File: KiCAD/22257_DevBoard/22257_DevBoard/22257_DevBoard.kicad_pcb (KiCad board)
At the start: 6 copper layers, 5 parts, among them U3 TPS73633DBV, U4 TPS562202, U5 INA219AxD, U6 INA219AxD, U7 BME680

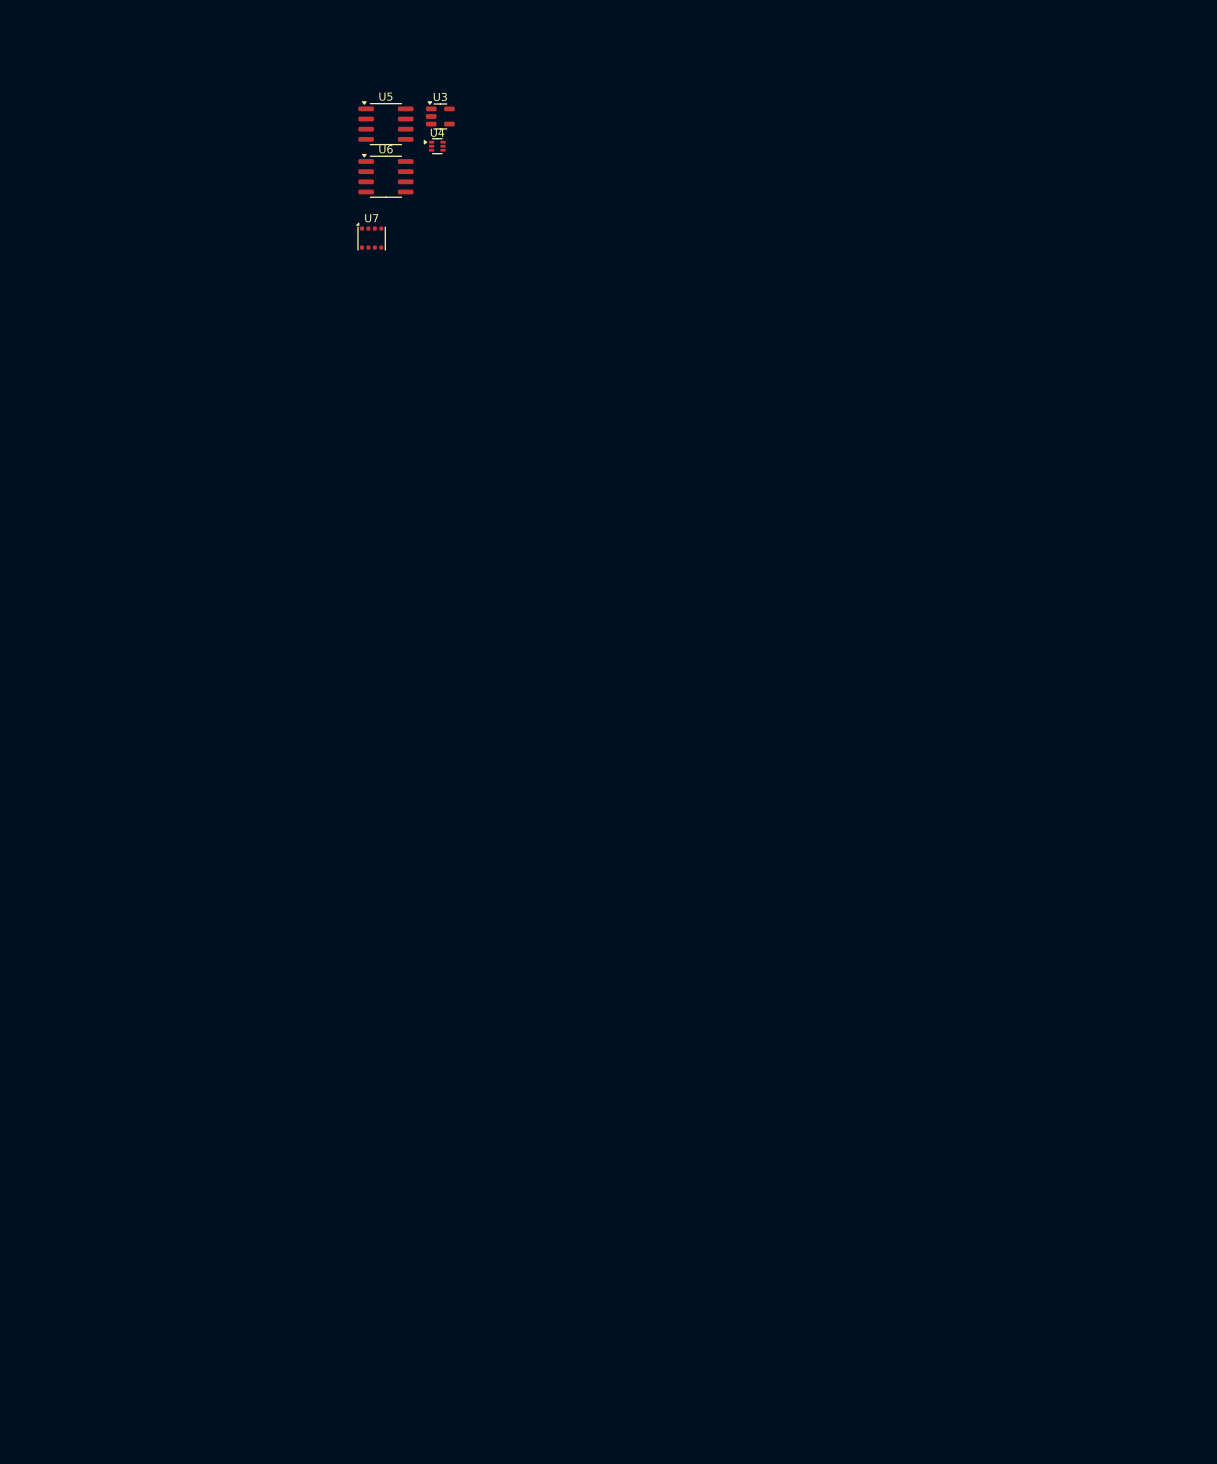
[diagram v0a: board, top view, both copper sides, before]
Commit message: Started layout
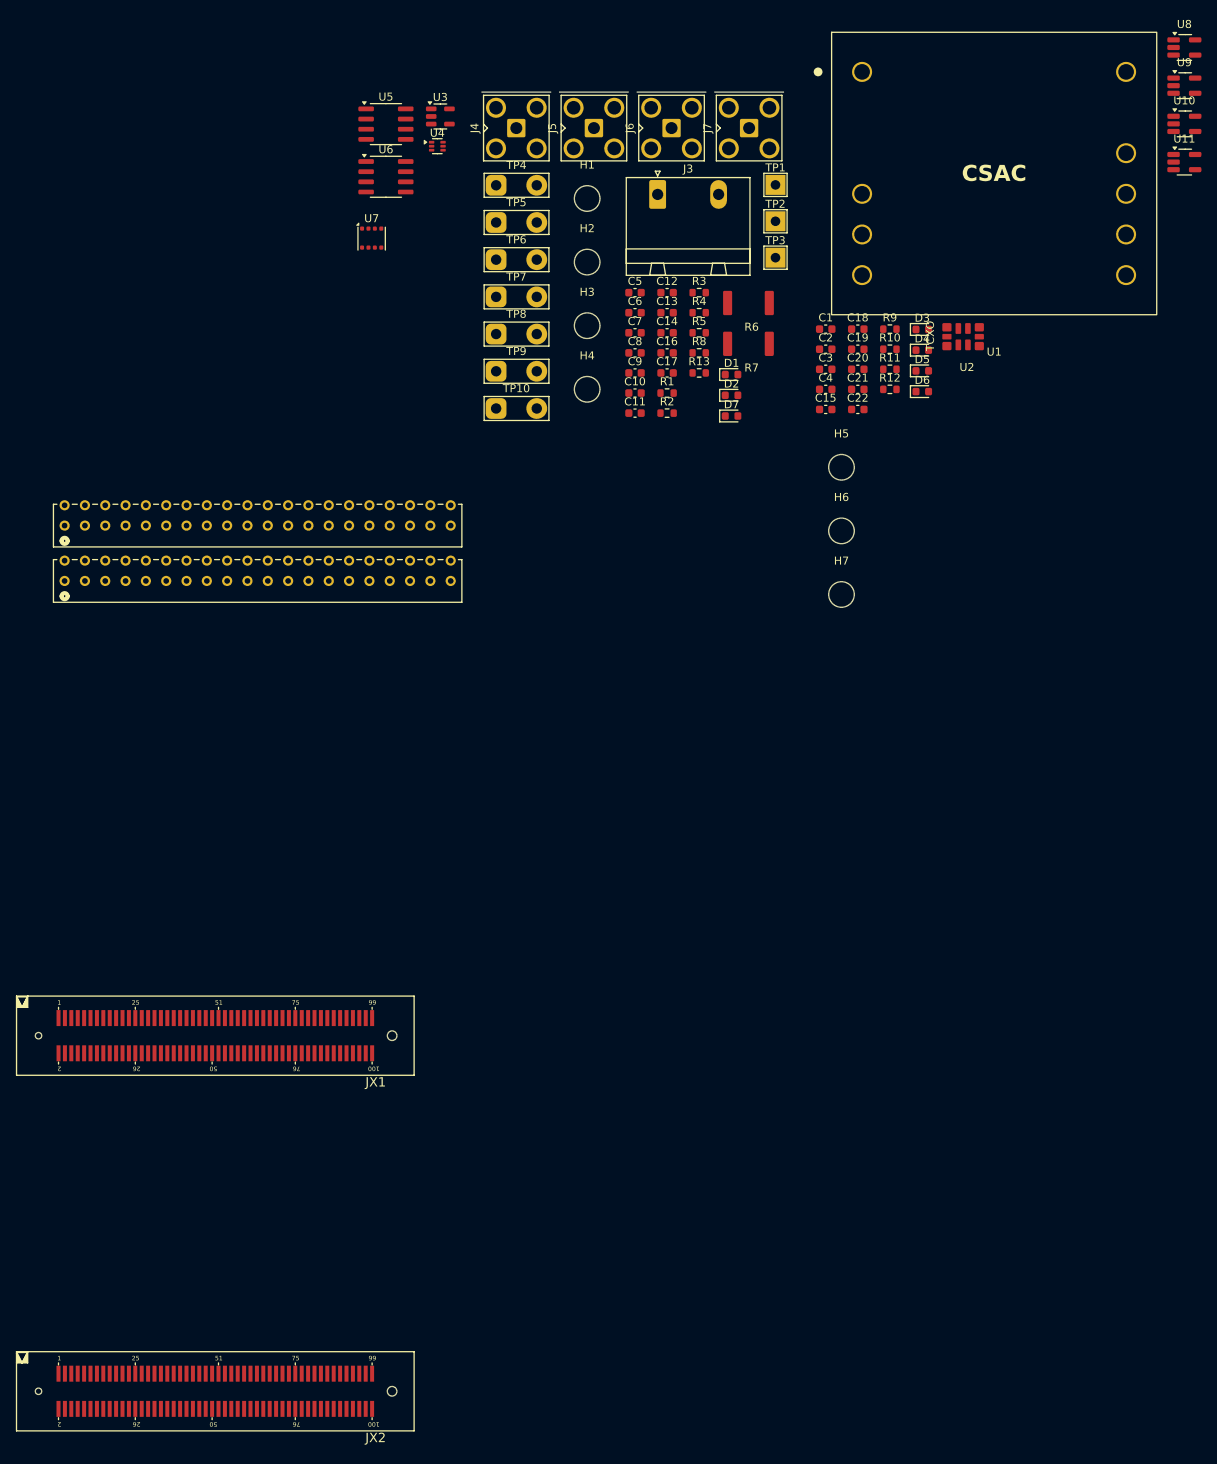
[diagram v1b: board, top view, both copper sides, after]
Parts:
- added C1: 0.01u, Capacitor_SMD:C_0603_1608Metric, F.Cu at (58.7, 28.5)
- added C10: 0.1u, Capacitor_SMD:C_0603_1608Metric, F.Cu at (34.9, 36.5)
- added C11: 22u, Capacitor_SMD:C_0603_1608Metric, F.Cu at (34.9, 39.0)
- added C12: 22u, Capacitor_SMD:C_0603_1608Metric, F.Cu at (38.9, 23.9)
- added C13: 22u, Capacitor_SMD:C_0603_1608Metric, F.Cu at (38.9, 26.4)
- added C14: .1u, Capacitor_SMD:C_0603_1608Metric, F.Cu at (38.9, 28.9)
- added C15: 4.7u, Capacitor_SMD:C_0603_1608Metric, F.Cu at (58.7, 38.5)
- added C16: 0.01u, Capacitor_SMD:C_0603_1608Metric, F.Cu at (38.9, 31.4)
- added C17: 0.01u, Capacitor_SMD:C_0603_1608Metric, F.Cu at (38.9, 34.0)
- added C18: 0.01u, Capacitor_SMD:C_0603_1608Metric, F.Cu at (62.7, 28.5)
- added C19: 0.01u, Capacitor_SMD:C_0603_1608Metric, F.Cu at (62.7, 31.0)
- added C2: 4.7u, Capacitor_SMD:C_0603_1608Metric, F.Cu at (58.7, 31.0)
- added C20: 0.01u, Capacitor_SMD:C_0603_1608Metric, F.Cu at (62.7, 33.5)
- added C21: 0.01u, Capacitor_SMD:C_0603_1608Metric, F.Cu at (62.7, 36.0)
- added C22: 0.01u, Capacitor_SMD:C_0603_1608Metric, F.Cu at (62.7, 38.5)
- added C3: 4.7u, Capacitor_SMD:C_0603_1608Metric, F.Cu at (58.7, 33.5)
- added C4: 0.01u, Capacitor_SMD:C_0603_1608Metric, F.Cu at (58.7, 36.0)
- added C5: 10n, Capacitor_SMD:C_0603_1608Metric, F.Cu at (34.9, 23.9)
- added C6: 10u, Capacitor_SMD:C_0603_1608Metric, F.Cu at (34.9, 26.4)
- added C7: 0.1u, Capacitor_SMD:C_0603_1608Metric, F.Cu at (34.9, 28.9)
- added C8: 10u, Capacitor_SMD:C_0603_1608Metric, F.Cu at (34.9, 31.4)
- added C9: 4.7u, Capacitor_SMD:C_0603_1608Metric, F.Cu at (34.9, 34.0)
- added D1: LED, LED_SMD:LED_0603_1608Metric, F.Cu at (46.9, 34.2)
- added D2: LED, LED_SMD:LED_0603_1608Metric, F.Cu at (46.9, 36.8)
- added D3: LED, LED_SMD:LED_0603_1608Metric, F.Cu at (70.8, 28.5)
- added D4: LED, LED_SMD:LED_0603_1608Metric, F.Cu at (70.8, 31.1)
- added D5: LED, LED_SMD:LED_0603_1608Metric, F.Cu at (70.8, 33.7)
- added D6: LED, LED_SMD:LED_0603_1608Metric, F.Cu at (70.8, 36.3)
- added D7: LED, LED_SMD:LED_0603_1608Metric, F.Cu at (46.9, 39.3)
- added H1: MOUNT-PAD-ROUND5.0, MountingHole:MountingHole_3.2mm_M3, F.Cu at (28.9, 12.2)
- added H2: MOUNT-PAD-ROUND5.0, MountingHole:MountingHole_3.2mm_M3, F.Cu at (28.9, 20.1)
- added H3: MOUNT-PAD-ROUND5.0, MountingHole:MountingHole_3.2mm_M3, F.Cu at (28.9, 28.1)
- added H4: MOUNT-PAD-ROUND5.0, MountingHole:MountingHole_3.2mm_M3, F.Cu at (28.9, 36.0)
- added H5: MOUNT-PAD-ROUND5.0, MountingHole:MountingHole_3.2mm_M3, F.Cu at (60.7, 45.8)
- added H6: MOUNT-PAD-ROUND5.0, MountingHole:MountingHole_3.2mm_M3, F.Cu at (60.7, 53.7)
- added H7: MOUNT-PAD-ROUND5.0, MountingHole:MountingHole_3.2mm_M3, F.Cu at (60.7, 61.6)
- added J1: TD-120-G-AACON40_2X20_TU_HTS_SAI, 22257_DevBoard:CON40_2X20_TU_HTS_SAI, F.Cu at (-12.3, 51.8)
- added J2: TD-120-G-AACON40_2X20_TU_HTS_SAI, 22257_DevBoard:CON40_2X20_TU_HTS_SAI, F.Cu at (-12.3, 58.7)
- added J3: Screw_Terminal_01x02, Connector_Phoenix_GMSTB:PhoenixContact_GMSTBA_2,5_2-G-7,62_1x02_P7.62mm_Horizontal, F.Cu at (37.7, 11.6)
- added J4: Conn_Coaxial, Connector_Coaxial:SMA_Amphenol_901-143_Horizontal, F.Cu at (20.0, 3.35)
- added J5: Conn_Coaxial, Connector_Coaxial:SMA_Amphenol_901-143_Horizontal, F.Cu at (29.7, 3.35)
- added J6: Conn_Coaxial, Connector_Coaxial:SMA_Amphenol_901-143_Horizontal, F.Cu at (39.4, 3.35)
- added J7: Conn_Coaxial, Connector_Coaxial:SMA_Amphenol_901-143_Horizontal, F.Cu at (49.1, 3.35)
- added JX1: 61083-102402LF, 22257_DevBoard:61083-102402LF_1104291, F.Cu at (-39.7, 116.8)
- added JX2: 61083-102402LF, 22257_DevBoard:61083-102402LF_1104291, F.Cu at (-39.7, 161.3)
- added R1: 200k, Resistor_SMD:R_0603_1608Metric, F.Cu at (38.9, 36.5)
- added R10: 1k, Resistor_SMD:R_0603_1608Metric, F.Cu at (66.7, 31.0)
- added R11: 1k, Resistor_SMD:R_0603_1608Metric, F.Cu at (66.7, 33.5)
- added R12: 1k, Resistor_SMD:R_0603_1608Metric, F.Cu at (66.7, 36.0)
- added R13: 1k, Resistor_SMD:R_0603_1608Metric, F.Cu at (42.9, 34.0)
- added R2: 1k, Resistor_SMD:R_0603_1608Metric, F.Cu at (38.9, 39.0)
- added R3: 10k, Resistor_SMD:R_0603_1608Metric, F.Cu at (42.9, 23.9)
- added R4: 52.3k, Resistor_SMD:R_0603_1608Metric, F.Cu at (42.9, 26.4)
- added R5: 10k, Resistor_SMD:R_0603_1608Metric, F.Cu at (42.9, 28.9)
- added R6: R_Shunt_US, 2222_DevBoar_Footprints:BVT-I-R0002-1, F.Cu at (46.4, 25.2)
- added R7: R_Shunt_US, 2222_DevBoar_Footprints:BVT-I-R0002-1, F.Cu at (46.4, 30.3)
- added R8: 1k, Resistor_SMD:R_0603_1608Metric, F.Cu at (42.9, 31.4)
- added R9: 1k, Resistor_SMD:R_0603_1608Metric, F.Cu at (66.7, 28.5)
- added TP1: TestPoint, TestPoint:TestPoint_THTPad_2.5x2.5mm_Drill1.2mm, F.Cu at (52.4, 10.4)
- added TP10: TestPoint_2Pole, TestPoint:TestPoint_2Pads_Pitch5.08mm_Drill1.3mm, F.Cu at (17.5, 38.4)
- added TP2: TestPoint, TestPoint:TestPoint_THTPad_2.5x2.5mm_Drill1.2mm, F.Cu at (52.4, 15.0)
- added TP3: TestPoint, TestPoint:TestPoint_THTPad_2.5x2.5mm_Drill1.2mm, F.Cu at (52.4, 19.6)
- added TP4: TestPoint_2Pole, TestPoint:TestPoint_2Pads_Pitch5.08mm_Drill1.3mm, F.Cu at (17.5, 10.5)
- added TP5: TestPoint_2Pole, TestPoint:TestPoint_2Pads_Pitch5.08mm_Drill1.3mm, F.Cu at (17.5, 15.2)
- added TP6: TestPoint_2Pole, TestPoint:TestPoint_2Pads_Pitch5.08mm_Drill1.3mm, F.Cu at (17.5, 19.8)
- added TP7: TestPoint_2Pole, TestPoint:TestPoint_2Pads_Pitch5.08mm_Drill1.3mm, F.Cu at (17.5, 24.4)
- added TP8: TestPoint_2Pole, TestPoint:TestPoint_2Pads_Pitch5.08mm_Drill1.3mm, F.Cu at (17.5, 29.1)
- added TP9: TestPoint_2Pole, TestPoint:TestPoint_2Pads_Pitch5.08mm_Drill1.3mm, F.Cu at (17.5, 33.8)
- added U1: ~, 2222_DevBoar_Footprints:SA-45, F.Cu at (63.2, -3.67)
- added U10: 74LVC1G17, Package_TO_SOT_SMD:SOT-23-5_HandSoldering, F.Cu at (103.5, 2.83)
- added U11: 74LVC1G17, Package_TO_SOT_SMD:SOT-23-5_HandSoldering, F.Cu at (103.5, 7.60)
- added U2: ~, 2222_DevBoar_Footprints:SiT5356, F.Cu at (73.8, 28.2)
- added U8: 74LVC1G17, Package_TO_SOT_SMD:SOT-23-5_HandSoldering, F.Cu at (103.5, -6.72)
- added U9: 74LVC1G17, Package_TO_SOT_SMD:SOT-23-5_HandSoldering, F.Cu at (103.5, -1.95)

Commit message: Finished Component Placement and Arrangement.
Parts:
- removed H5, H6, H7: MOUNT-PAD-ROUND5.0, MountingHole:MountingHole_3.2mm_M3
- added H10: MountingHole_Pad, MountingHole:MountingHole_3.2mm_M3_Pad, F.Cu at (12.8, 19.1)
- added H11: MountingHole_Pad, MountingHole:MountingHole_3.2mm_M3_Pad, F.Cu at (12.8, 68.6)
- added H8: MountingHole_Pad, MountingHole:MountingHole_3.2mm_M3_Pad, F.Cu at (106.8, 68.6)
- added H9: MountingHole_Pad, MountingHole:MountingHole_3.2mm_M3_Pad, F.Cu at (106.8, 19.1)
- added L1: 10u, Inductor_SMD:L_Bourns-SRU8043, F.Cu at (149.3, 2.62)
- added L2: 4.7u, Inductor_SMD:L_Bourns-SRU8043, F.Cu at (166.2, 2.79)
- added TP11: TestPoint, TestPoint:TestPoint_THTPad_2.5x2.5mm_Drill1.2mm, F.Cu at (162.8, 33.3)
- added TP12: TestPoint, TestPoint:TestPoint_THTPad_2.5x2.5mm_Drill1.2mm, F.Cu at (97.8, 81.3)
- added TP13: TestPoint, TestPoint:TestPoint_THTPad_2.5x2.5mm_Drill1.2mm, F.Cu at (29.2, 5.54)
- added TP14: TestPoint, TestPoint:TestPoint_THTPad_2.5x2.5mm_Drill1.2mm, F.Cu at (104.3, 1.56)
- added TP15: TestPoint, TestPoint:TestPoint_THTPad_2.5x2.5mm_Drill1.2mm, F.Cu at (155.7, 25.7)
- added TP16: TestPoint, TestPoint:TestPoint_THTPad_2.5x2.5mm_Drill1.2mm, F.Cu at (155.7, 29.7)
- added TP17: TestPoint, TestPoint:TestPoint_THTPad_2.5x2.5mm_Drill1.2mm, F.Cu at (128.5, 22.1)
- added TP18: TestPoint, TestPoint:TestPoint_THTPad_2.5x2.5mm_Drill1.2mm, F.Cu at (128.5, 26.2)
- H1, H2, H3, H4: value MOUNT-PAD-ROUND5.0 -> MountingHole_Pad; footprint MountingHole:MountingHole_3.2mm_M3 -> MountingHole:MountingHole_3.2mm_M3_Pad
- moved J4 183.2 mm to (201.9, 25.4), turned to -90 degrees
- moved TP5 182.8 mm to (193.0, 66.0), turned to -90 degrees
- moved H4 182.2 mm to (203.2, 88.9)
- moved TP4 180.1 mm to (193.0, 50.8), turned to -90 degrees
- moved H3 176.6 mm to (203.2, 0.00)
- moved TP7 176.3 mm to (193.0, 40.6), turned to 90 degrees
- moved J5 176.2 mm to (201.9, 40.6), turned to -90 degrees
- moved TP6 175.6 mm to (193.0, 25.4), turned to 90 degrees
- moved J6 170.7 mm to (201.9, 55.9), turned to -90 degrees
- moved U7 170.7 mm to (171.4, 37.5), turned to 180 degrees
- moved TP8 167.6 mm to (184.4, 14.0)
- moved J7 167.1 mm to (201.9, 71.1), turned to -90 degrees
- moved JX2 161.1 mm to (40.6, 21.6)
- moved U4 160.5 mm to (170.6, 8.80), turned to -90 degrees
- moved U5 158.7 mm to (160.8, 25.4), turned to 90 degrees
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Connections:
- U5 pad 1: unconnected-(U5-A1-Pad1) -> Net-(U5-A1)
- U5 pad 2: unconnected-(U5-A0-Pad2) -> Net-(U5-A0)
- U6 pad 1: unconnected-(U6-A1-Pad1) -> Net-(U6-A1)
- U6 pad 2: unconnected-(U6-A0-Pad2) -> Net-(U6-A0)

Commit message: Routed Breakouts
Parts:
- turned J1 to 180 degrees
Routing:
- net /MicroZed_Headers/34_W14: track 0.00 -> 29.6 mm, vias 0 -> 1
- net /MicroZed_Headers/34_T19: track 0.00 -> 27.7 mm, vias 0 -> 1
- net /MicroZed_Headers/34_V16: track 0.00 -> 27.7 mm, vias 0 -> 1
- net /MicroZed_Headers/34_R14: track 0.00 -> 27.2 mm, vias 0 -> 1
- net /MicroZed_Headers/34_P16: track 0.00 -> 26.9 mm, vias 0 -> 1
- net /MicroZed_Headers/34_W19: track 0.00 -> 26.5 mm, vias 0 -> 1
- net PM_SCL_5V: track 0.00 -> 26.5 mm, vias 0 -> 1
- net /MicroZed_Headers/34_T12: track 0.00 -> 26.4 mm, vias 0 -> 1
- net /MicroZed_Headers/34_W13: track 0.00 -> 26.3 mm, vias 0 -> 1
- net /MicroZed_Headers/34_W16: track 0.00 -> 26.3 mm, vias 0 -> 1
- net /MicroZed_Headers/34_U12: track 0.00 -> 26.3 mm, vias 0 -> 1
- net /MicroZed_Headers/34_P15: track 0.00 -> 26.1 mm, vias 0 -> 1
- net /MicroZed_Headers/34_T17: track 0.00 -> 25.9 mm, vias 0 -> 1
- net /MicroZed_Headers/34_W18: track 0.00 -> 25.7 mm, vias 0 -> 1
- net /MicroZed_Headers/35_G14: track 0.00 -> 25.7 mm, vias 0 -> 1
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- added copper zone on F.Cu, net +5V
- added copper zone on In1.Cu, net GND
- added copper zone on In3.Cu, net GND

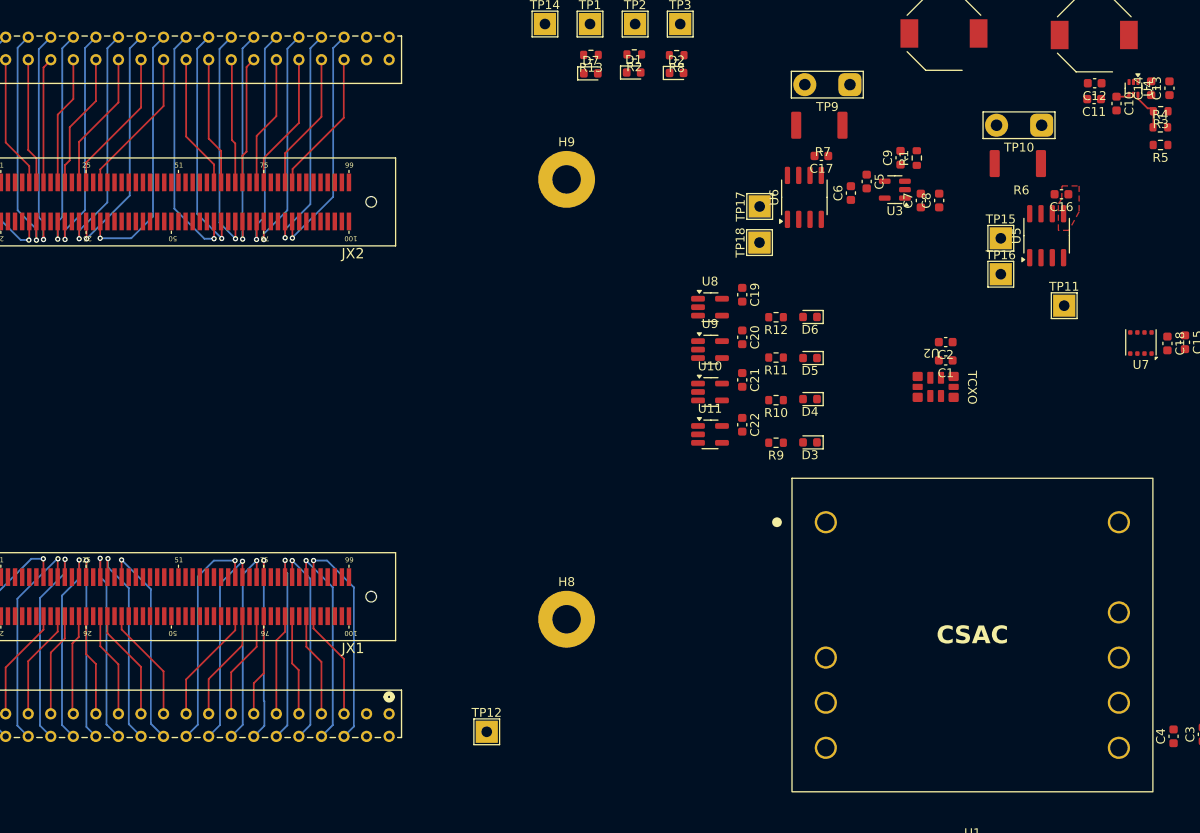
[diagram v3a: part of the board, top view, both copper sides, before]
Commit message: A lot of routing progress done
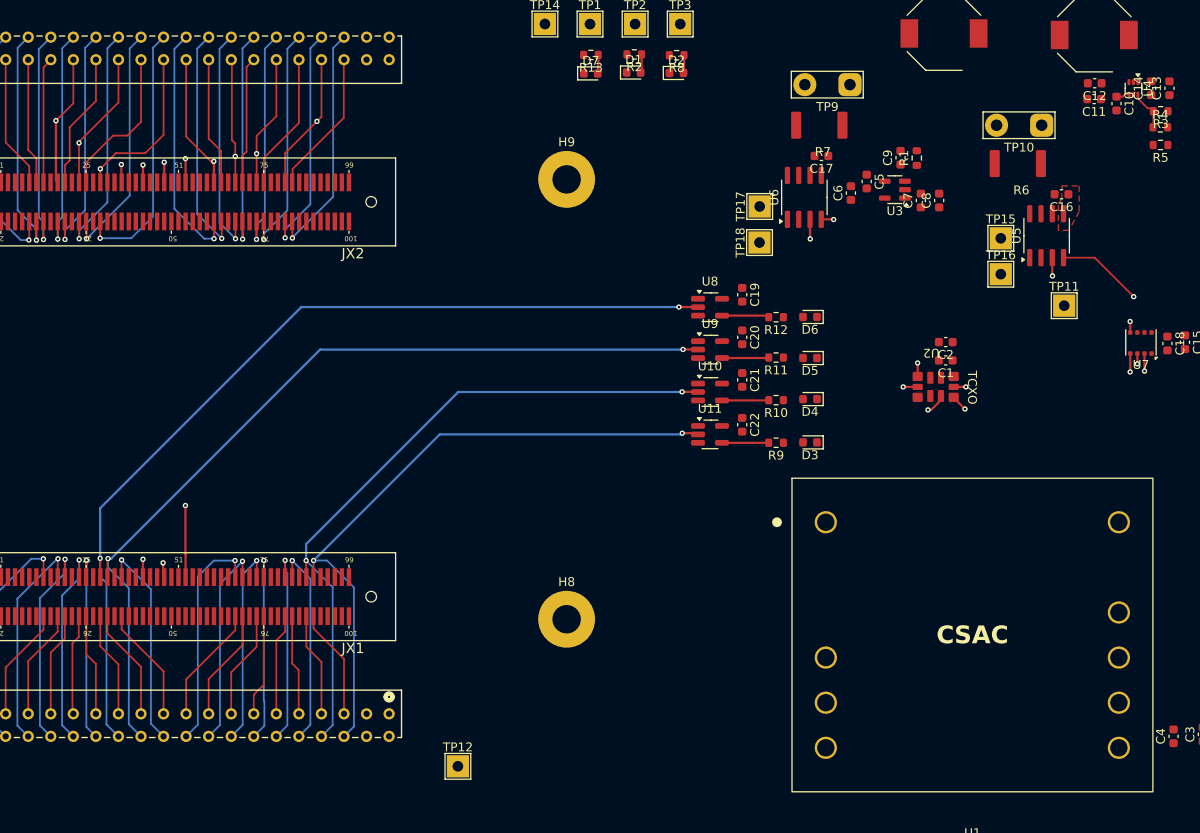
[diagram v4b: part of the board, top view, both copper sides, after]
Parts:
- moved TP12 5.06 mm to (94.5, 85.1)
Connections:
- J1 pad 28: /MicroZed_Headers/35_D18 -> BRD_PPS_IN
- J2 pad 31: /MicroZed_Headers/34_V18 -> BRD_10MHz_OUT
- JX1 pad 25: /MicroZed_Headers/35_D18 -> BRD_PPS_IN
- JX1 pad 47: CSAC_BITE -> CSAC_PPS_OUT
- JX2 pad 53: unconnected-(JX2-BANK34_T20-Pad53) -> TCXO_A0
- JX2 pad 75: /MicroZed_Headers/34_V18 -> BRD_10MHz_OUT
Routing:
- net ES_CSB: track 16.8 -> 174.0 mm, vias 0 -> 2
- net ES_SDI: track 0.00 -> 147.8 mm, vias 0 -> 2
- net ES_SCK: track 0.00 -> 140.4 mm, vias 0 -> 2
- net ES_SDO: track 0.00 -> 136.4 mm, vias 0 -> 2
- net CSAC_PPS_IN: track 23.1 -> 158.4 mm
- net CSAC_PPS_OUT: track 0.00 -> 121.9 mm, vias 0 -> 1
- net CSAC_RF_OUT: track 0.00 -> 114.3 mm, vias 0 -> 1
- net TCXO_A0: track 0.00 -> 113.6 mm, vias 0 -> 2
- net TCXO_SCL: track 15.1 -> 113.3 mm, vias 0 -> 2
- net PM_SCL_3v3: track 15.7 -> 113.4 mm, vias 0 -> 2
- net PM_SDA_3v3: track 14.5 -> 111.9 mm, vias 0 -> 2
- net TCXO_OE: track 14.0 -> 109.9 mm, vias 0 -> 2
- net CSAC_Rx: track 23.8 -> 111.8 mm
- net TCXO_SDA: track 15.5 -> 102.4 mm, vias 0 -> 2
- net TCXO_10MHz: track 14.7 -> 100.4 mm, vias 0 -> 2
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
